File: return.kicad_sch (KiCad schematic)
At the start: 44 parts, among them IC1 LC709203F/MH, Q3 MOSFET-P, SW1 SWITCH_TACT_SMT4.6X2.8, SW2 SWITCH_TACT_SMT4.6X2.8, U1 ESP32-S3-MINI-1, U2 VREG_SOT23-5, U3 MCP73831/2, U4 BME280, U5 VREG_SOT23-5, X1 JSTPH, X3 USB_C

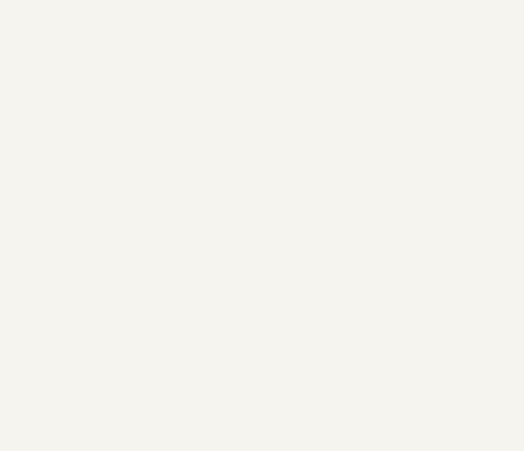
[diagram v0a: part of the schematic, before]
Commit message: Add keyboard-layout-editor json
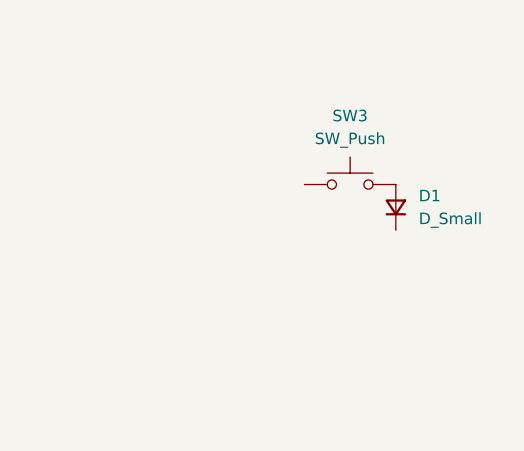
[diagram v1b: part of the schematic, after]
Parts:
- added D1: D_Small, symbol Device:D_Small
- added SW3: SW_Push, symbol Switch:SW_Push
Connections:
- new net: D1.2 (A), SW3.2
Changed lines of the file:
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@@
 	)
 	(symbol
+		(lib_id "Device:D_Small")
+		(at 327.66 39.37 90)
+		(unit 1)
+		(exclude_from_sim no)
+		(in_bom yes)
+		(on_board yes)
+		(dnp no)
+		(fields_autoplaced yes)
+		(property "Reference" "D1"
+			(at 330.2 38.0999 90)
+			(effects
+				(font
+					(size 1.27 1.27)
+				)
+				(justify right)
+			)
+		)
+		(property "Value" "D_Small"
+			(at 330.2 40.6399 90)
+			(effects
+				(font
+					(size 1.27 1.27)
+				)
+				(justify right)
+			)
+		)
+		(property "Footprint" ""
+			(at 327.66 39.37 90)
+			(effects
+				(font
+					(size 1.27 1.27)
+				)
+				(hide yes)
+			)
+		)
+		(property "Datasheet" "~"
+			(at 327.66 39.37 90)
+			(effects
+				(font
+					(size 1.27 1.27)
+				)
+				(hide yes)
+			)
+		)
+		(property "Description" "Diode, small symbol"
+			(at 327.66 39.37 0)
+			(effects
+				(font
+					(size 1.27 1.27)
+				)
+				(hide yes)
+			)
+		)
+		(property "Sim.Device" "D"
+			(at 327.66 39.37 0)
+			(effects
+				(font
+					(size 1.27 1.27)
+				)
+				(hide yes)
+			)
+		)
+		(property "Sim.Pins" "1=K 2=A"
+			(at 327.66 39.37 0)
+			(effects
+				(font
+					(size 1.27 1.27)
+				)
+				(hide yes)
+			)
+		)
+		(pin "2"
+		)
+		(pin "1"
+		)
+		(instances
+			(project ""
+				(path "/90d2660c-887d-46a9-be76-39f6378d1609"
+					(reference "D1")
+					(unit 1)
+				)
+			)
+		)
+	)
+	(symbol
 		(lib_id "return-eagle-import:adafruit_power_VBAT")
 		(at 43.18 25.4 0)
@@
 					(unit 1)
 				)
+			)
+		)
+	)
+	(symbol
+		(lib_id "Switch:SW_Push")
+		(at 322.58 36.83 0)
+		(unit 1)
+		(exclude_from_sim no)
+		(in_bom yes)
+		(on_board yes)
+		(dnp no)
+		(fields_autoplaced yes)
+		(property "Reference" "SW3"
+			(at 322.58 29.21 0)
+			(effects
+				(font
+					(size 1.27 1.27)
+				)
+			)
+		)
+		(property "Value" "SW_Push"
+			(at 322.58 31.75 0)
+			(effects
+				(font
+					(size 1.27 1.27)
+				)
+			)
+		)
+		(property "Footprint" ""
+			(at 322.58 31.75 0)
+			(effects
+				(font
+					(size 1.27 1.27)
+				)
+				(hide yes)
+			)
+		)
+		(property "Datasheet" "~"
+			(at 322.58 31.75 0)
+			(effects
+				(font
+					(size 1.27 1.27)
+				)
+				(hide yes)
+			)
+		)
+		(property "Description" "Push button switch, generic, two pins"
+			(at 324.866 40.64 0)
+			(effects
+				(font
+					(size 1.27 1.27)
+				)
+				(hide yes)
+			)
+		)
+		(pin "2"
+		)
+		(pin "1"
+		)
+		(instances
+			(project ""
+				(path "/90d2660c-887d-46a9-be76-39f6378d1609"
+					(reference "SW3")
+					(unit 1)
+				)

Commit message: Revise Schematic
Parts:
- added D10, D11, D12, D13, D14, D15, D16, D17, D18, D19, D2, D20, D21, D22, D23, D24, D25, D26, D27, D28, D29, D30, D31, D32, D33, D34, D35, D36, D37, D38, D39, D40, D41, D42, D43, D44, D45, D46, D47, D48, D49, D5, D50, D51, D52, D53, D54, D55, D56, D57, D58, D59, D6, D60, D61, D7, D8, D9: D_Small, symbol Device:D_Small
- added SW10, SW11, SW12, SW13, SW14, SW15, SW16, SW17, SW18, SW19, SW20, SW21, SW22, SW23, SW24, SW25, SW26, SW27, SW28, SW29, SW30, SW31, SW32, SW33, SW34, SW35, SW36, SW37, SW38, SW39, SW4, SW40, SW41, SW42, SW43, SW44, SW45, SW46, SW47, SW48, SW49, SW5, SW50, SW51, SW52, SW53, SW54, SW55, SW56, SW57, SW58, SW59, SW6, SW60, SW61, SW7, SW8, SW9: SW_Push, symbol Switch:SW_Push
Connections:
- net ROW0: now reaches D1.1 (K)
- net ROW0: now also D2.1 (K), D5.1 (K), D6.1 (K), D7.1 (K), D8.1 (K)
- net COL0: now reaches SW3.1
- net COL0: now also SW17.1, SW18.1, SW19.1, SW20.1
- new net: D33.2 (A), SW33.2
- new net: D58.2 (A), SW58.2
- new net: D39.2 (A), SW39.2
- new net: D48.2 (A), SW48.2
- new net: D60.2 (A), SW60.2
- new net: D10.2 (A), SW10.2
- new net: D11.1 (K), D12.1 (K), D13.1 (K), D14.1 (K), D15.1 (K), D16.1 (K)
- new net: D14.2 (A), SW14.2
- new net: D20.2 (A), SW20.2
- new net: D8.2 (A), SW8.2
- new net: D11.2 (A), SW11.2
- new net: D53.2 (A), SW53.2
- new net: D28.2 (A), SW28.2
- new net: D50.2 (A), SW50.2
- new net: D38.2 (A), SW38.2
- new net: D47.2 (A), SW47.2
- new net: D9.2 (A), SW9.2
- new net: D35.2 (A), SW35.2
- new net: D41.2 (A), SW41.2
- new net: D45.2 (A), SW45.2
- new net: D22.2 (A), SW22.2
- new net: D24.2 (A), SW24.2
- new net: D61.2 (A), SW61.2
- new net: D5.2 (A), SW5.2
- new net: D44.2 (A), SW44.2
- new net: D55.2 (A), SW55.2
- new net: D19.2 (A), SW19.2
- new net: D12.2 (A), SW12.2
- new net: D6.2 (A), SW6.2
- new net: D37.2 (A), SW37.2
- new net: D27.2 (A), SW27.2
- new net: D52.2 (A), SW52.2
- new net: D29.2 (A), SW29.2
- new net: D31.2 (A), SW31.2
- new net: D21.2 (A), SW21.2
- new net: D15.2 (A), SW15.2
- new net: D46.2 (A), SW46.2
- new net: D30.2 (A), SW30.2
- new net: D26.2 (A), SW26.2
- new net: D59.2 (A), SW59.2
- new net: D43.2 (A), SW43.2
- new net: D18.2 (A), SW18.2
- new net: D23.2 (A), SW23.2
- new net: D7.2 (A), SW7.2
- new net: D56.2 (A), SW56.2
- new net: D40.2 (A), SW40.2
- new net: D17.2 (A), SW17.2
- new net: D13.2 (A), SW13.2
- new net: D42.2 (A), SW42.2
- new net: D57.2 (A), SW57.2
- new net: D51.2 (A), SW51.2
- new net: D32.2 (A), SW32.2
- new net: D36.2 (A), SW36.2
- new net: D34.2 (A), SW34.2
- new net: D25.2 (A), SW25.2
- new net: D2.2 (A), SW4.2
- new net: D54.2 (A), SW54.2
- new net: D16.2 (A), SW16.2
- new net: D49.2 (A), SW49.2
- new net COL1: SW25.1, SW26.1, SW27.1, SW4.1, SW9.1
- new net COL10: SW10.1, SW15.1, SW52.1, SW53.1, SW54.1
- new net COL11: SW16.1, SW21.1, SW22.1, SW23.1, SW24.1
- new net COL2: SW28.1, SW29.1, SW30.1, SW5.1, SW55.1
- new net COL3: SW31.1, SW32.1, SW33.1, SW56.1, SW6.1
- new net COL4: SW34.1, SW35.1, SW36.1, SW57.1, SW7.1
- new net COL5: SW37.1, SW38.1, SW39.1, SW58.1, SW8.1
- new net COL6: SW11.1, SW40.1, SW41.1, SW42.1, SW59.1
- new net COL7: SW12.1, SW43.1, SW44.1, SW45.1, SW60.1
- new net COL8: SW13.1, SW46.1, SW47.1, SW48.1, SW61.1
- new net COL9: SW14.1, SW49.1, SW50.1, SW51.1
- new net ROW1: D17.1 (K), D21.1 (K), D25.1 (K), D28.1 (K), D31.1 (K), D34.1 (K), D37.1 (K), D40.1 (K), D43.1 (K), D46.1 (K), D49.1 (K), D52.1 (K)
- new net ROW2: D18.1 (K), D23.1 (K), D26.1 (K), D29.1 (K), D32.1 (K), D35.1 (K), D38.1 (K), D41.1 (K), D44.1 (K), D47.1 (K), D50.1 (K), D53.1 (K)
- new net ROW3: D19.1 (K), D24.1 (K), D27.1 (K), D30.1 (K), D33.1 (K), D36.1 (K), D39.1 (K), D42.1 (K), D45.1 (K), D48.1 (K), D51.1 (K), D54.1 (K)
- new net ROW4: D10.1 (K), D20.1 (K), D55.1 (K), D56.1 (K), D57.1 (K), D58.1 (K), D59.1 (K), D60.1 (K), D61.1 (K), D9.1 (K)

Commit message: add project for numpad, finish PCB routing.
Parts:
- removed C1, C2, C3, C6, C7, C8, C9: CAP_CERAMIC0805-NOOUTLINE, return:0805-NO, symbol return-eagle-import:microbuilder_CAP_CERAMIC0805-NOOUTLINE
- removed C10, C4, C5: CAP_CERAMIC0603_NO, return:0603-NO, symbol return-eagle-import:microbuilder_CAP_CERAMIC0603_NO
- removed C11: CAP_CERAMIC_0805MP, return:_0805MP, symbol return-eagle-import:microbuilder_CAP_CERAMIC_0805MP
- removed CHG0, D3: LED0603_NOOUTLINE, return:CHIPLED_0603_NOOUTLINE, symbol return-eagle-import:microbuilder_LED0603_NOOUTLINE
- removed CONN1: JST SH, return:JST_SH4_RA, symbol return-eagle-import:microbuilder_STEMMA_I2C_QTRA
- removed D4: DIODE-SCHOTTKYSOD-123, return:SOD-123, symbol return-eagle-import:microbuilder_DIODE-SCHOTTKYSOD-123
- removed IC1: LC709203F/MH, return:WLCSP9, symbol return-eagle-import:LC709203F/MH
- removed JP1: HEADER-1X16ROUND, return:1X16_ROUND, symbol return-eagle-import:microbuilder_HEADER-1X16ROUND
- removed JP3: HEADER-1X12, return:1X12_ROUND, symbol return-eagle-import:microbuilder_HEADER-1X12
- removed LED1: WS2812B_SK6805_1515, return:SK6805_1515, symbol return-eagle-import:microbuilder_WS2812B_SK6805_1515
- removed Q3: MOSFET-P, return:SOT23-R, symbol return-eagle-import:microbuilder_MOSFET-P
- removed R1, R10, R12, R17, R2, R4, R5, R7, R8: RESISTOR_0603_NOOUT, return:0603-NO, symbol return-eagle-import:microbuilder_RESISTOR_0603_NOOUT
- removed R3: RESISTOR_4PACK, return:RESPACK_4X0603, symbol return-eagle-import:microbuilder_RESISTOR_4PACK
- removed SW1, SW2: SWITCH_TACT_SMT4.6X2.8, return:BTN_KMR2_4.6X2.8, symbol return-eagle-import:microbuilder_SWITCH_TACT_SMT4.6X2.8
- removed TP1: TESTPOINTROUND1.5MMNO, return:TESTPOINT_ROUND_1.5MM_NO, symbol return-eagle-import:TESTPOINTROUND1.5MMNO
- removed U$31, U$32: MOUNTINGHOLE2.5, return:MOUNTINGHOLE_2.5_PLATED, symbol return-eagle-import:microbuilder_MOUNTINGHOLE2.5
- removed U$34, U$35: FIDUCIAL_1MM, return:FIDUCIAL_1MM, symbol return-eagle-import:microbuilder_FIDUCIAL_1MM
- removed U1: ESP32-S3-MINI-1, return:QFN60_ESP32-S2-MINI-1_EXP, symbol return-eagle-import:ESP32-S3-MINI-1
- removed U2, U5: VREG_SOT23-5, return:SOT23-5, symbol return-eagle-import:microbuilder_VREG_SOT23-5
- removed U3: MCP73831/2, return:SOT23-5, symbol return-eagle-import:microbuilder_MCP73831/2
- removed U4: BME280, return:BME280, symbol return-eagle-import:BME280
- removed X1: JSTPH, return:JSTPH2_BATT, symbol return-eagle-import:adafruit_electromech_CON_JST_PH_2PIN_MT_BATT
- removed X3: USB_C, return:USB_C_CUSB31-CFM2AX-01-X, symbol return-eagle-import:adafruit_connector_USB_C
- added A1: Adafruit_Feather_Generic, Module:Adafruit_Feather, symbol MCU_Module:Adafruit_Feather_Generic
- added J1: Conn_01x04, Connector_PinHeader_2.54mm:PinHeader_1x04_P2.54mm_Vertical, symbol Connector_Generic:Conn_01x04
- added J10, J11, J12, J13, J14, J15, J16, J17, J18, J19, J2, J3, J4, J5, J6, J7, J8, J9: Conn_01x01, symbol Connector_Generic:Conn_01x01
- added LED0, LED10, LED11, LED12, LED13, LED14, LED15, LED16, LED17, LED18, LED19, LED2, LED20, LED23, LED24, LED25, LED26, LED27, LED28, LED29, LED3, LED30, LED31, LED32, LED33, LED34, LED37, LED38, LED39, LED4, LED40, LED41, LED42, LED43, LED44, LED45, LED46, LED47, LED48, LED5, LED51, LED52, LED53, LED54, LED55, LED56, LED57, LED59, LED6, LED60, LED61, LED63, LED66, LED67, LED68, LED7, LED70, LED8, LED9: SK6812MINI, Keebio-Parts:SK6812-MINI-E, symbol LED:SK6812MINI
- D1, D10, D11, D12, D13, D14, D15, D16, D17, D18, D19, D2, D20, D21, D22, D23, D24, D25, D26, D27, D28, D29, D30, D31, D32, D33, D34, D35, D36, D37, D38, D39, D40, D41, D42, D43, D44, D45, D46, D47, D48, D49, D5, D50, D51, D52, D53, D54, D55, D56, D57, D58, D59, D6, D60, D61, D7, D8, D9: footprint (none) -> Diode_THT:D_DO-35_SOD27_P7.62mm_Horizontal
- SW10, SW11, SW12, SW13, SW14, SW15, SW16, SW17, SW18, SW19, SW20, SW21, SW22, SW23, SW24, SW25, SW26, SW27, SW28, SW29, SW3, SW30, SW31, SW32, SW33, SW34, SW35, SW36, SW37, SW38, SW39, SW4, SW40, SW41, SW42, SW43, SW44, SW45, SW46, SW47, SW48, SW49, SW5, SW50, SW51, SW52, SW53, SW54, SW55, SW56, SW57, SW58, SW59, SW6, SW60, SW61, SW7, SW8, SW9: footprint (none) -> Kailh_PG1353_Hotswap:Kailh-PG1353-Hotswap-1U
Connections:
- net COL0: now also A1.10 (A5), J2.1 (Pin_1)
- net COL1: now also A1.11 (SCK), J3.1 (Pin_1), J8.1 (Pin_1)
- net COL10: now also A1.21 (D2), J14.1 (Pin_1), J9.1 (Pin_1)
- net COL11: now also A1.20 (D1), J15.1 (Pin_1)
- net COL2: now also A1.12 (MOSI), J4.1 (Pin_1)
- net COL3: now also A1.13 (MISO), J5.1 (Pin_1)
- net COL4: now also A1.14 (RX), J6.1 (Pin_1)
- net COL5: now also A1.15 (TX), J7.1 (Pin_1)
- net COL6: now also A1.25 (D6), J10.1 (Pin_1)
- net COL7: now also A1.24 (D5), J11.1 (Pin_1)
- net COL8: now also A1.23 (D4), J12.1 (Pin_1)
- net COL9: now also A1.22 (D3), J13.1 (Pin_1)
- net GND: now also A1.4 (GND), J1.1 (Pin_1), LED0.2 (VSS), LED10.2 (VSS), LED11.2 (VSS), LED12.2 (VSS), LED13.2 (VSS), LED14.2 (VSS), LED15.2 (VSS), LED16.2 (VSS), LED17.2 (VSS), LED18.2 (VSS), LED19.2 (VSS), LED2.2 (VSS), LED20.2 (VSS), LED23.2 (VSS), LED24.2 (VSS), LED25.2 (VSS), LED26.2 (VSS), LED27.2 (VSS), LED28.2 (VSS), LED29.2 (VSS), LED3.2 (VSS), LED30.2 (VSS), LED31.2 (VSS), LED32.2 (VSS), LED33.2 (VSS), LED34.2 (VSS), LED37.2 (VSS), LED38.2 (VSS), LED39.2 (VSS), LED4.2 (VSS), LED40.2 (VSS), LED41.2 (VSS), LED42.2 (VSS), LED43.2 (VSS), LED44.2 (VSS), LED45.2 (VSS), LED46.2 (VSS), LED47.2 (VSS), LED48.2 (VSS), LED5.2 (VSS), LED51.2 (VSS), LED52.2 (VSS), LED53.2 (VSS), LED54.2 (VSS), LED55.2 (VSS), LED56.2 (VSS), LED57.2 (VSS), LED59.2 (VSS), LED6.2 (VSS), LED60.2 (VSS), LED61.2 (VSS), LED63.2 (VSS), LED66.2 (VSS), LED67.2 (VSS), LED68.2 (VSS), LED7.2 (VSS), LED70.2 (VSS), LED8.2 (VSS), LED9.2 (VSS)
- net ROW0: now also D11.1 (K), D12.1 (K), D13.1 (K), D14.1 (K), D15.1 (K), D16.1 (K), A1.5 (A0), J16.1 (Pin_1)
- net ROW1: now also A1.6 (A1), J17.1 (Pin_1)
- net ROW2: now also D22.1 (K), A1.7 (A2), J18.1 (Pin_1); no longer D23.1 (K)
- net ROW3: now also D23.1 (K), A1.8 (A3), J19.1 (Pin_1); no longer D24.1 (K)
- net ROW4: now also D24.1 (K), A1.9 (A4)
- new net: LED67.1 (DOUT), LED68.3 (DIN)
- new net: LED66.1 (DOUT), LED67.3 (DIN)
- new net: A1.18 (SCL), J1.2 (Pin_2)
- new net: A1.17 (SDA), J1.3 (Pin_3)
- new net: LED29.1 (DOUT), LED30.3 (DIN)
- new net: LED30.1 (DOUT), LED31.3 (DIN)
- new net: LED7.1 (DOUT), LED8.3 (DIN)
- new net: LED6.1 (DOUT), LED7.3 (DIN)
- new net: LED10.3 (DIN), LED9.1 (DOUT)
- new net: LED8.1 (DOUT), LED9.3 (DIN)
- new net: LED60.1 (DOUT), LED61.3 (DIN)
- new net: LED59.1 (DOUT), LED60.3 (DIN)
- new net: LED13.1 (DOUT), LED14.3 (DIN)
- new net: LED51.1 (DOUT), LED52.3 (DIN)
- new net: LED48.1 (DOUT), LED51.3 (DIN)
- new net: LED55.1 (DOUT), LED56.3 (DIN)
- new net: LED41.1 (DOUT), LED42.3 (DIN)
- new net: LED46.1 (DOUT), LED47.3 (DIN)
- new net: LED45.1 (DOUT), LED46.3 (DIN)
- new net: LED15.1 (DOUT), LED16.3 (DIN)
- new net: LED43.1 (DOUT), LED44.3 (DIN)
- new net: LED63.1 (DOUT), LED66.3 (DIN)
- new net: LED11.1 (DOUT), LED12.3 (DIN)
- new net: LED10.1 (DOUT), LED11.3 (DIN)
- new net: LED44.1 (DOUT), LED45.3 (DIN)
- new net: LED12.1 (DOUT), LED13.3 (DIN)
- new net: LED47.1 (DOUT), LED48.3 (DIN)
- new net: LED4.1 (DOUT), LED5.3 (DIN)
- new net: LED3.1 (DOUT), LED4.3 (DIN)
- new net: LED18.1 (DOUT), LED19.3 (DIN)
- new net: LED17.1 (DOUT), LED18.3 (DIN)
- new net: LED23.1 (DOUT), LED24.3 (DIN)
- new net: LED20.1 (DOUT), LED23.3 (DIN)
- new net: LED57.1 (DOUT), LED59.3 (DIN)
- new net: LED27.1 (DOUT), LED28.3 (DIN)
- new net: LED54.1 (DOUT), LED55.3 (DIN)
- new net: LED53.1 (DOUT), LED54.3 (DIN)
- new net: LED52.1 (DOUT), LED53.3 (DIN)
- new net: LED40.1 (DOUT), LED41.3 (DIN)
- new net: LED61.1 (DOUT), LED63.3 (DIN)
- new net: LED16.1 (DOUT), LED17.3 (DIN)
- new net: LED5.1 (DOUT), LED6.3 (DIN)
- new net: LED0.1 (DOUT), LED2.3 (DIN)
- new net: LED39.1 (DOUT), LED40.3 (DIN)
- new net: LED19.1 (DOUT), LED20.3 (DIN)
- new net: LED32.1 (DOUT), LED33.3 (DIN)
- new net: LED31.1 (DOUT), LED32.3 (DIN)
- new net: LED26.1 (DOUT), LED27.3 (DIN)
- new net: LED25.1 (DOUT), LED26.3 (DIN)
- new net: LED2.1 (DOUT), LED3.3 (DIN)
- new net: LED38.1 (DOUT), LED39.3 (DIN)
- new net: LED24.1 (DOUT), LED25.3 (DIN)
- new net: LED33.1 (DOUT), LED34.3 (DIN)
- new net: LED37.1 (DOUT), LED38.3 (DIN)
- new net: LED34.1 (DOUT), LED37.3 (DIN)
- new net: LED68.1 (DOUT), LED70.3 (DIN)
- new net +5V: A1.26 (USB), J1.4 (Pin_4), LED0.4 (VDD), LED10.4 (VDD), LED11.4 (VDD), LED12.4 (VDD), LED13.4 (VDD), LED14.4 (VDD), LED15.4 (VDD), LED16.4 (VDD), LED17.4 (VDD), LED18.4 (VDD), LED19.4 (VDD), LED2.4 (VDD), LED20.4 (VDD), LED23.4 (VDD), LED24.4 (VDD), LED25.4 (VDD), LED26.4 (VDD), LED27.4 (VDD), LED28.4 (VDD), LED29.4 (VDD), LED3.4 (VDD), LED30.4 (VDD), LED31.4 (VDD), LED32.4 (VDD), LED33.4 (VDD), LED34.4 (VDD), LED37.4 (VDD), LED38.4 (VDD), LED39.4 (VDD), LED4.4 (VDD), LED40.4 (VDD), LED41.4 (VDD), LED42.4 (VDD), LED43.4 (VDD), LED44.4 (VDD), LED45.4 (VDD), LED46.4 (VDD), LED47.4 (VDD), LED48.4 (VDD), LED5.4 (VDD), LED51.4 (VDD), LED52.4 (VDD), LED53.4 (VDD), LED54.4 (VDD), LED55.4 (VDD), LED56.4 (VDD), LED57.4 (VDD), LED59.4 (VDD), LED6.4 (VDD), LED60.4 (VDD), LED61.4 (VDD), LED63.4 (VDD), LED66.4 (VDD), LED67.4 (VDD), LED68.4 (VDD), LED7.4 (VDD), LED70.4 (VDD), LED8.4 (VDD), LED9.4 (VDD)
- new net LED_DIN: A1.19 (D0), LED0.3 (DIN)
- new net row1DOut: LED14.1 (DOUT), LED15.3 (DIN)
- new net row2DOut: LED28.1 (DOUT), LED29.3 (DIN)
- new net row3DOut: LED42.1 (DOUT), LED43.3 (DIN)
- new net row4DOut: LED56.1 (DOUT), LED57.3 (DIN)
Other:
- note removed: "1.0K = 1000mA"
- note removed: "10K = 100mA"
- note removed: "2.0K = 500mA"
- note removed: "5.0K = 200mA"
- note removed: "LED"
- note removed: "LIPO CHARGING"
- note removed: "NEOPIXEL"
- note removed: "POWER AND FILTERING"
- note removed: "PSRAMCS"
- note removed: "RESET"
- note removed: "USB TO SERIAL CONVERTER"
- moved on the sheet: D1, D10, D11, D12, D13, D14, D15, D16, D17, D18, D19, D2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

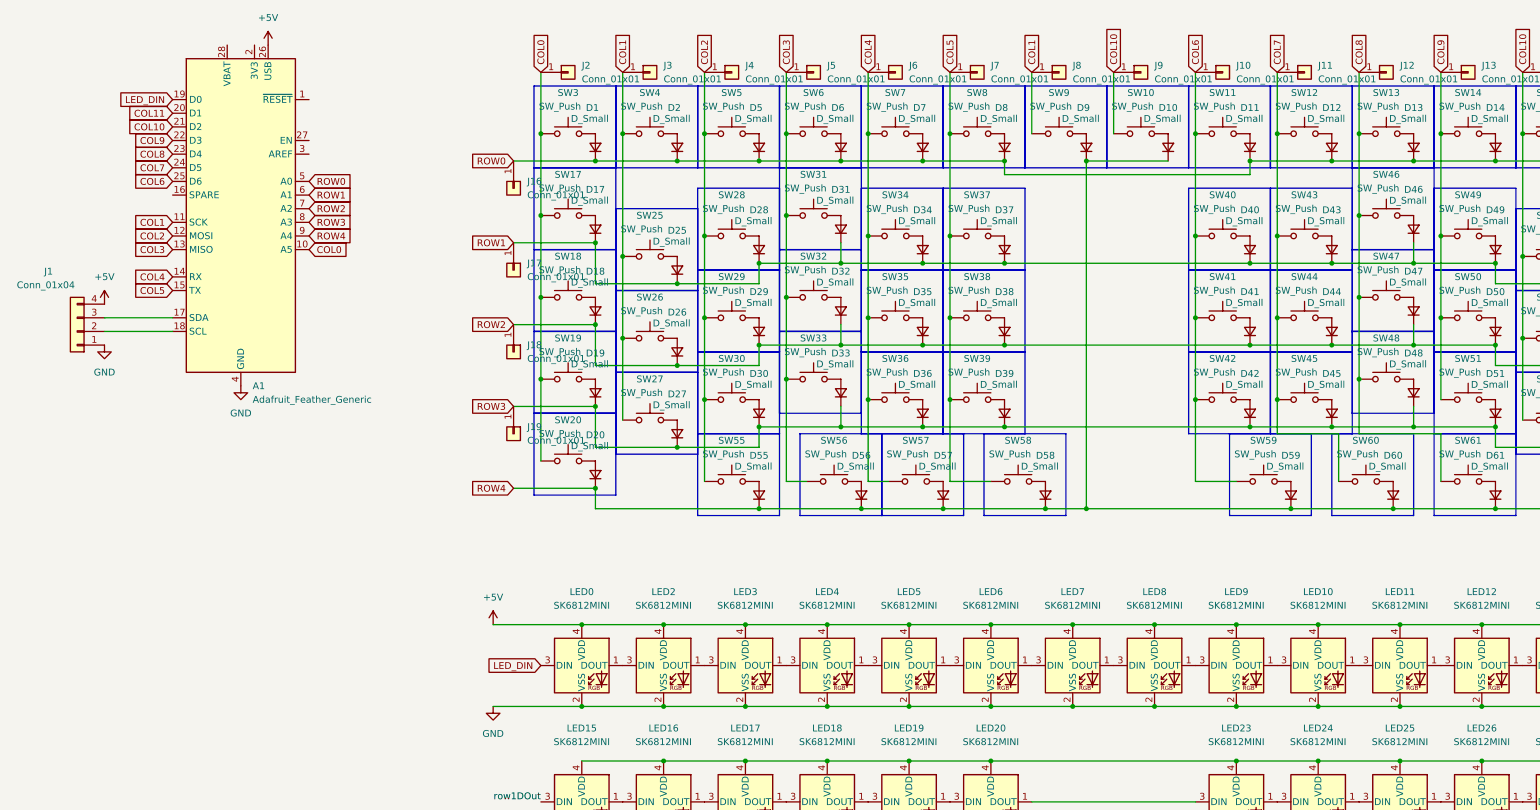
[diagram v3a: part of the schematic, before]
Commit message: Finish main schematic, finish aux schematic, add production files.
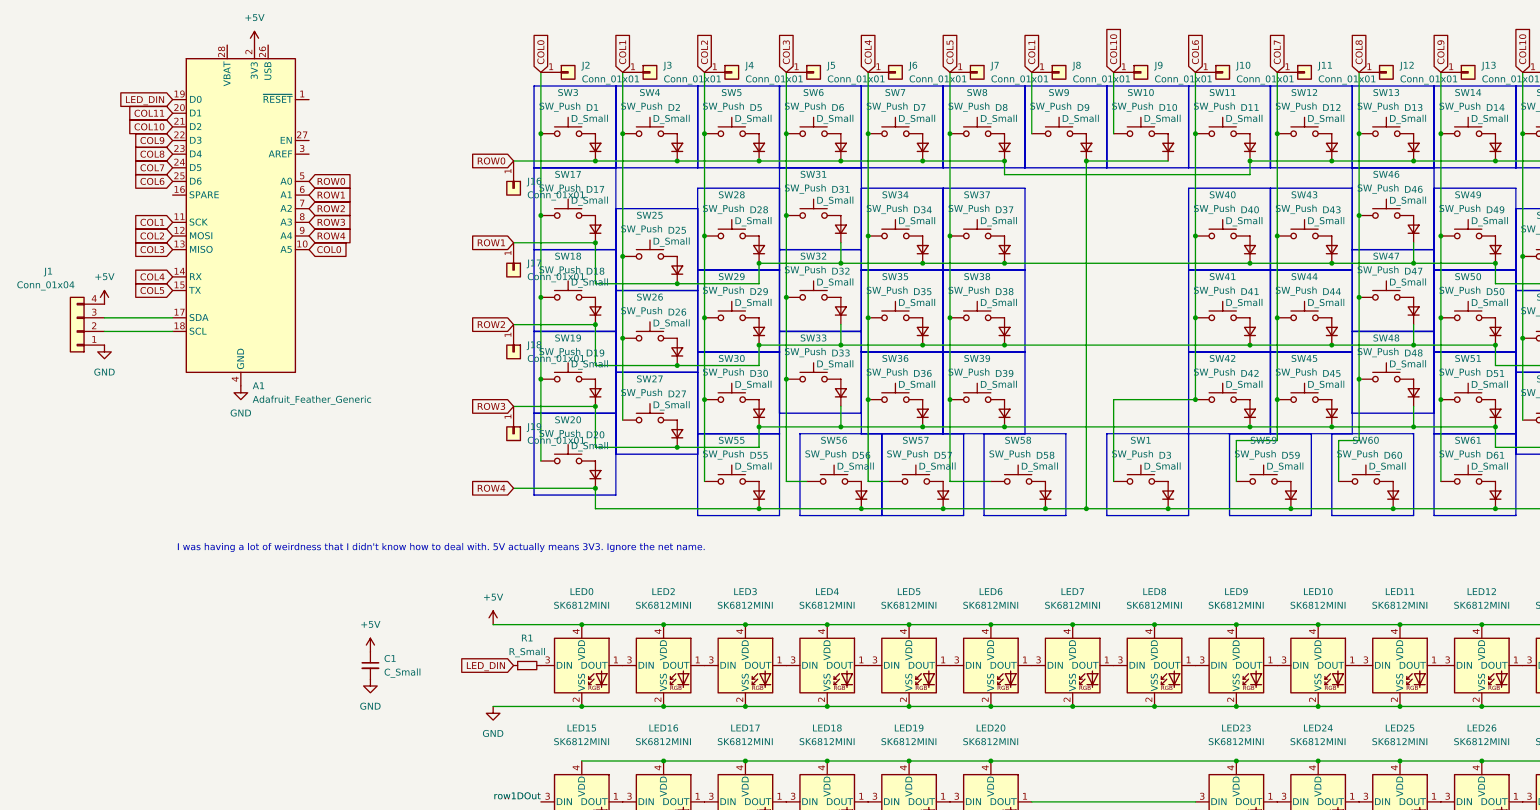
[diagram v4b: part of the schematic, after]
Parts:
- added C1: C_Small, Resistor_THT:R_Axial_DIN0204_L3.6mm_D1.6mm_P2.54mm_Vertical, symbol Device:C_Small
- added D3: D_Small, Diode_THT:D_DO-35_SOD27_P7.62mm_Horizontal, symbol Device:D_Small
- added R1: R_Small, Resistor_THT:R_Axial_DIN0207_L6.3mm_D2.5mm_P7.62mm_Horizontal, symbol Device:R_Small
- added SW1: SW_Push, Kailh_PG1353_Hotswap:Kailh-PG1353-Hotswap-1U, symbol Switch:SW_Push
- J2: footprint (none) -> Resistor_THT:R_Axial_DIN0207_L6.3mm_D2.5mm_P7.62mm_Horizontal
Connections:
- net +5V: now also A1.2 (3V3), C1.1; no longer A1.26 (USB)
- net COL6: now also SW1.1; no longer SW59.1
- net COL7: now also SW59.1; no longer SW60.1
- net COL8: now also SW60.1; no longer SW61.1
- net COL9: now also SW61.1
- net GND: now also C1.2
- net LED_DIN: now also R1.1; no longer LED0.3 (DIN)
- net ROW4: now also D3.1 (K)
- new net: D3.2 (A), SW1.2
- new net: LED0.3 (DIN), R1.2
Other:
- note added: "I was having a lot of weirdness that I didn't know how to deal with. 5V actually means 3V3. Ignore the net name."
